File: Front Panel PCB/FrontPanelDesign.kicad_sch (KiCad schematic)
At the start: 37 parts, among them J1 Conn_01x03_Pin, U1 TL081, U2 TL081, U3 TL081, U4 TL081, U5 TL081, U6 TL081

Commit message: Power Supplies Schematic Designed
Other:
- company: (none) -> University of Stellenbosch
- title: (none) -> Equiliser
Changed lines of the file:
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@@
 	(generator_version "10.0")
 	(paper "A3")
+	(title_block
+		(title "Equiliser")
+		(date "2026-06-02")
+		(rev "Rev A")
+		(company "University of Stellenbosch")
+		(comment 1 "Author: Karl Johan Hofmeyr")
+		(comment 2 "Skripsie Project")
+		(comment 3 "BEng - Mechatronic (4th Year)")
+	)
 	(junction
 		(at 306.07 104.14)

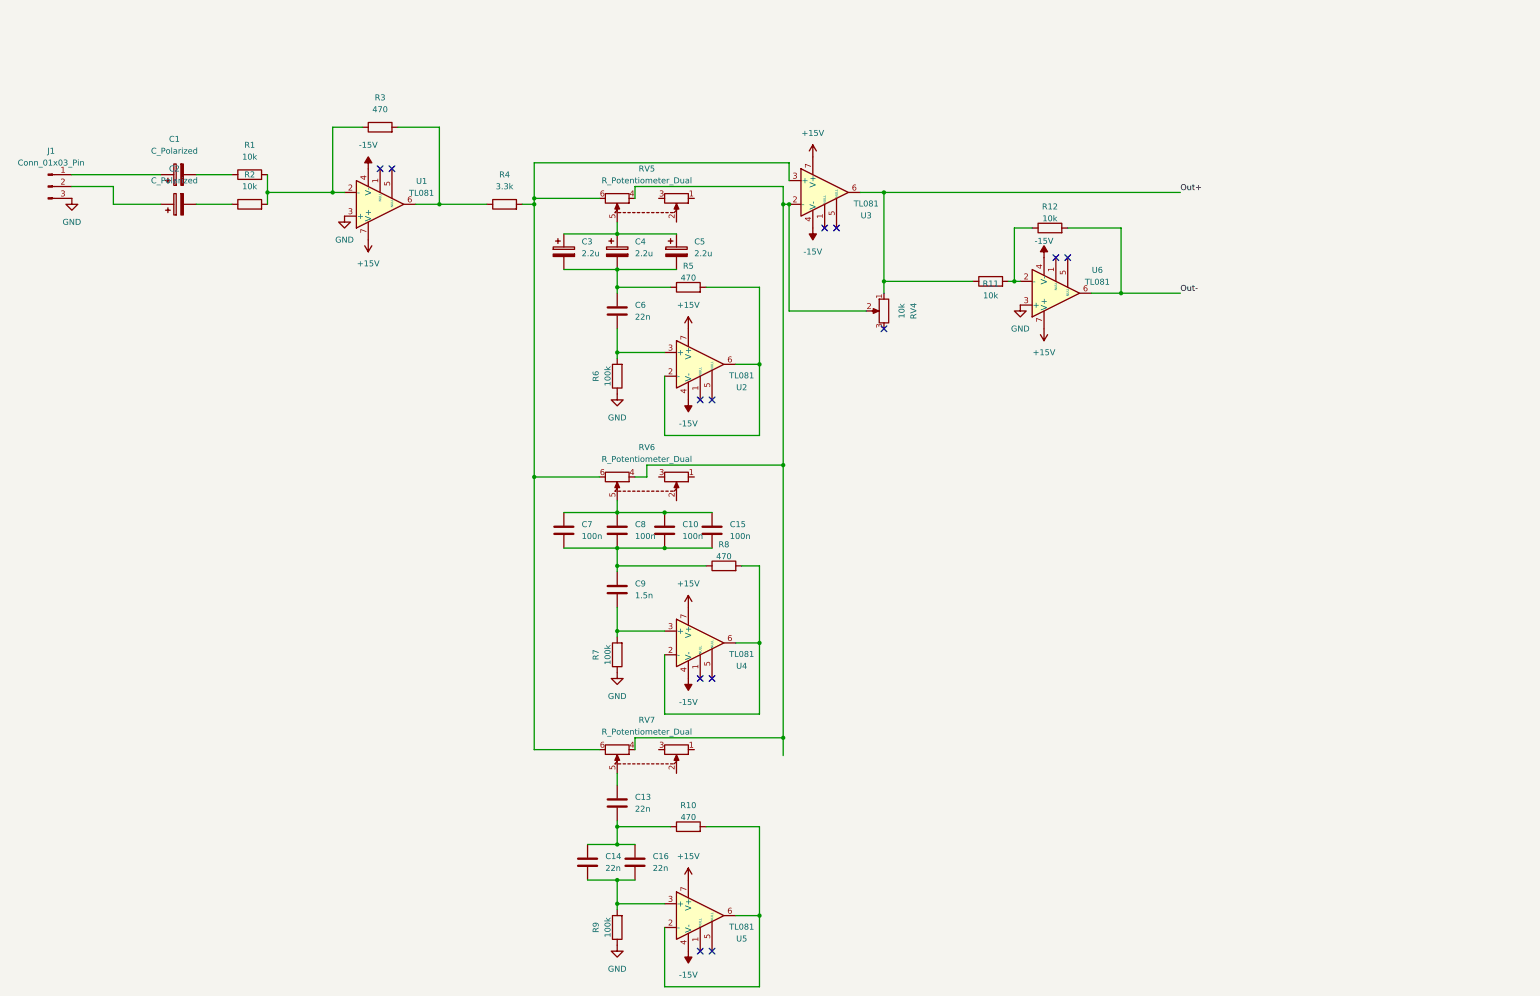
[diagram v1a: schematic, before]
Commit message: Output Stage Schematic Created and complete. Next: Integrate STM32
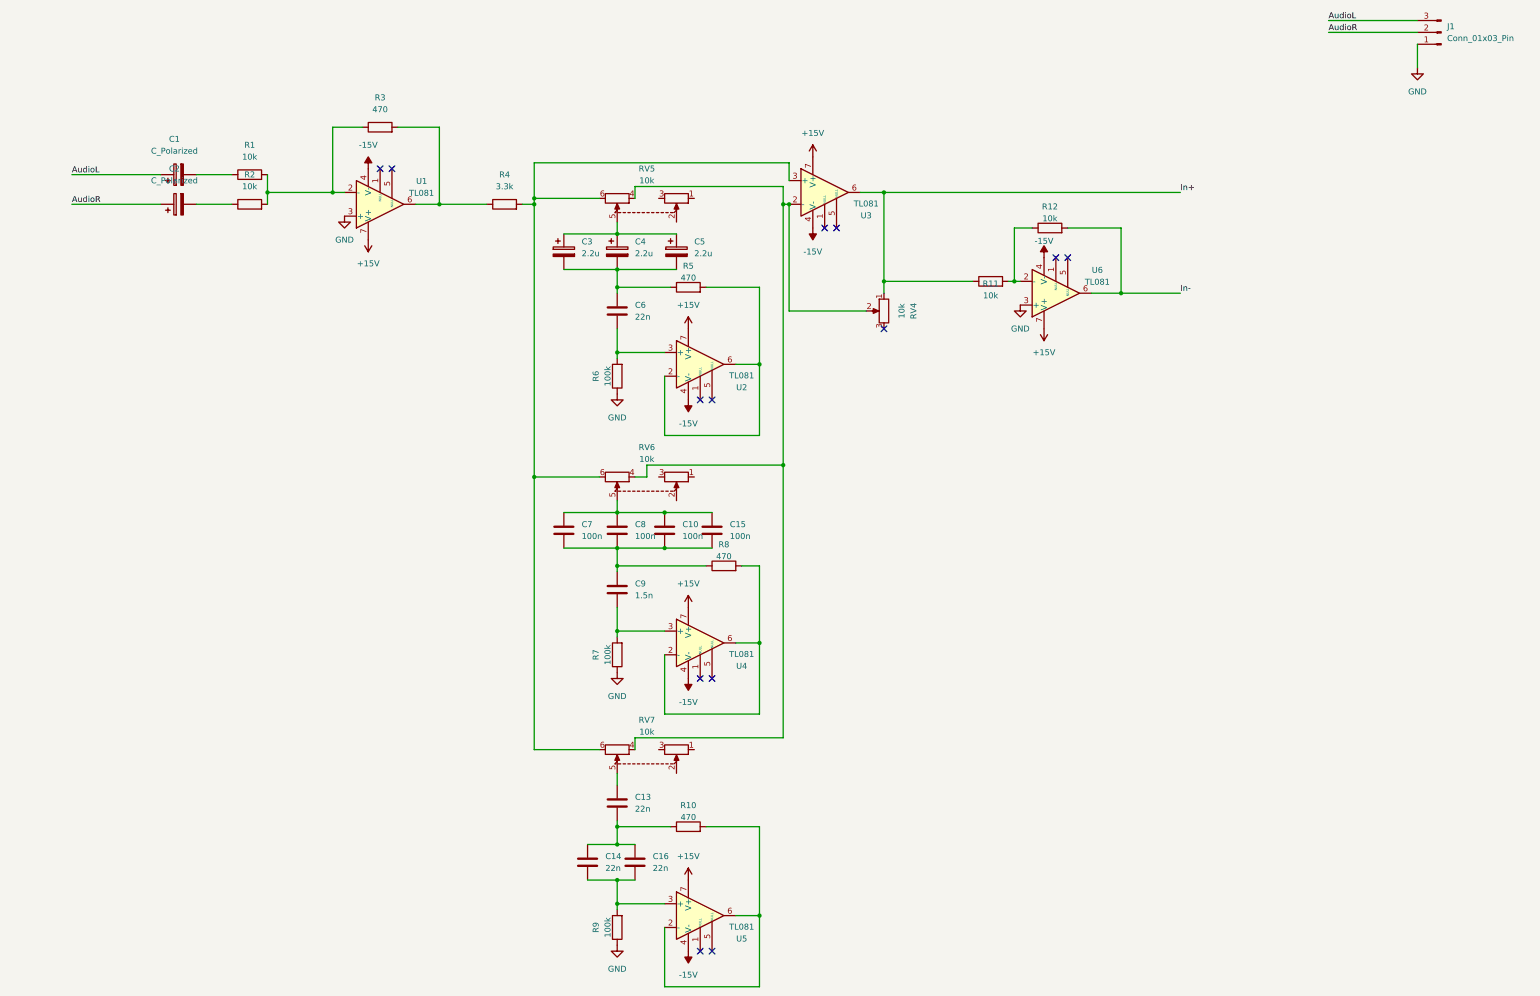
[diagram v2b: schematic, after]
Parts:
- RV5, RV6, RV7: value R_Potentiometer_Dual -> 10k
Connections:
- net GND: now also J1.1 (Pin_1); no longer J1.3 (Pin_3)
- net AudioL: now reaches C1.1
- net AudioL: now also J1.3 (Pin_3); no longer J1.1 (Pin_1)
- net AudioR: now reaches C2.1, J1.2 (Pin_2)
- net Out+ renamed In+
- net Out- renamed In-

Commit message: Bill of materials ETC finalised, selecting footprints next
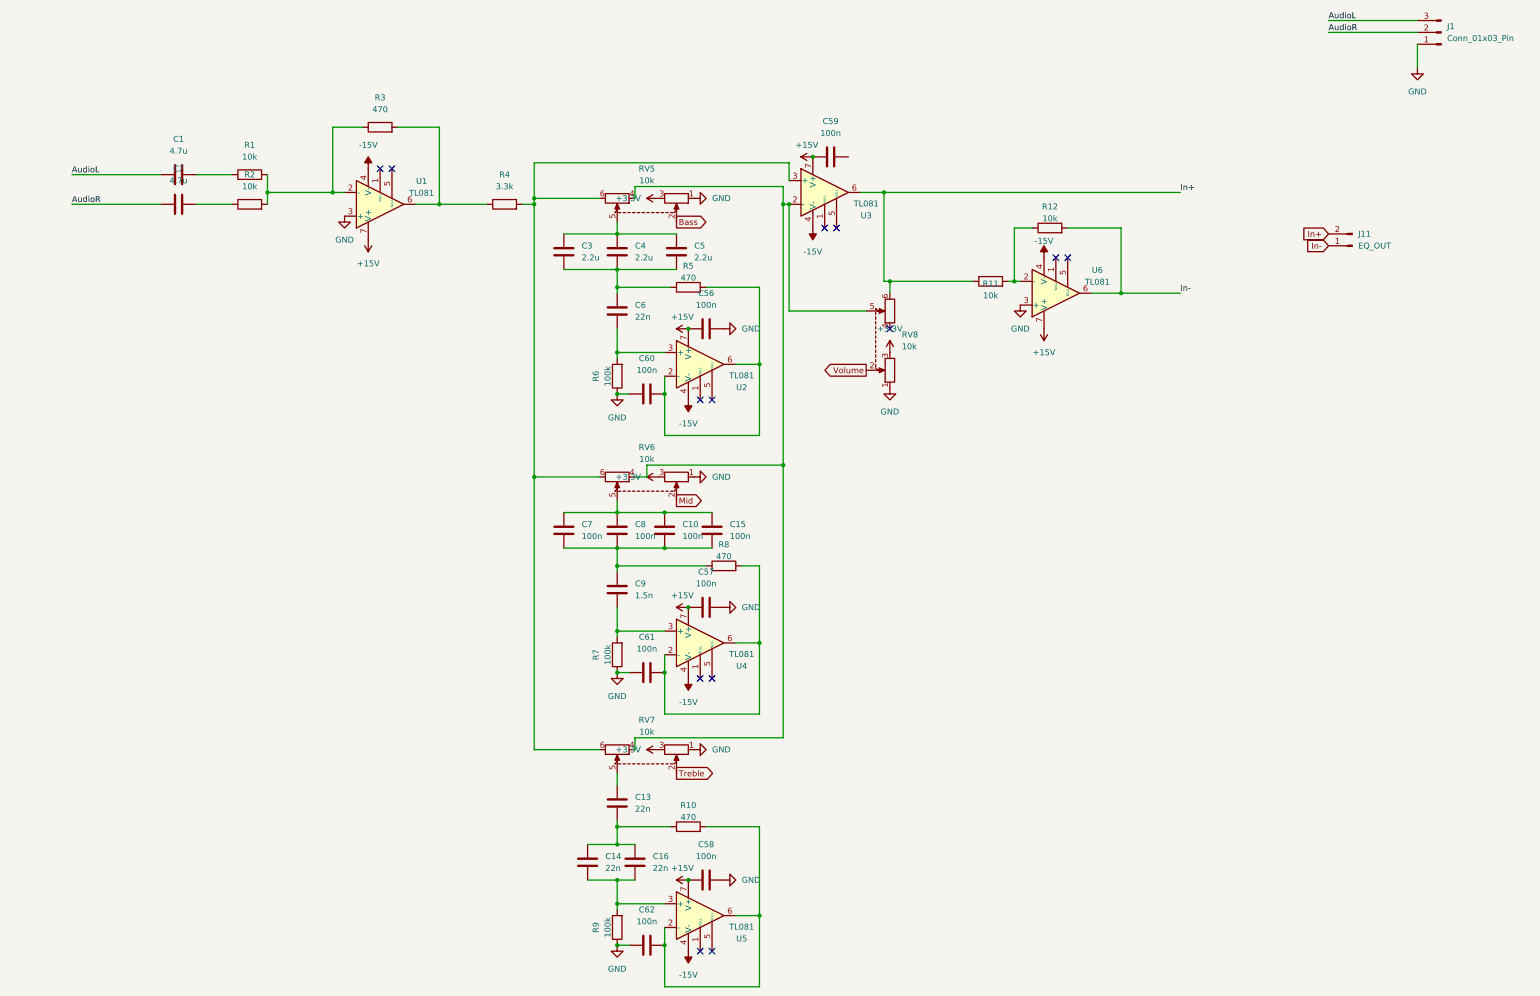
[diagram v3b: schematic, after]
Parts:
- removed C1, C2: C_Polarized, symbol Device:C_Polarized
- removed C3, C4, C5: 2.2u, symbol Device:C_Polarized
- removed RV4: 10k, symbol Device:R_Potentiometer
- added C1, C2: 4.7u, symbol Device:C
- added C3, C4, C5: 2.2u, symbol Device:C
- added C56, C57, C58, C59, C60, C61, C62: 100n, symbol Device:C
- added J11: EQ_OUT, symbol Connector:Conn_01x02_Pin
- added RV8: 10k, symbol Device:R_Potentiometer_Dual
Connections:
- net +15V: now also C56.2, C57.2, C58.2, C59.2
- net AudioL: now also C1.1
- net AudioR: now also C2.1
- net GND: now also RV5.1, RV6.1, RV7.1, C56.1, C57.1, C58.1, C60.2, C61.2, C62.2, RV8.1
- net In+: now also J11.2 (Pin_2), RV8.6
- net In-: now also J11.1 (Pin_1)
- net at R10.2, U5.2 (-), U5.6: now also C62.1
- net at RV5.4, RV6.4, RV7.4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: now also RV8.5
- net at C6.1, R5.1: now also C3.1, C4.1, C5.1
- net at RV5.5: now also C3.2, C4.2, C5.2
- net at R5.2, U2.2 (-), U2.6: now also C60.1
- net Treble: now reaches RV7.2
- net +3.3V: now reaches RV7.3
- net +3.3V: now also RV5.3, RV6.3, RV8.3
- net Bass: now reaches RV5.2
- net at R2.1: now also C2.2
- net Mid: now reaches RV6.2
- net at R8.2, U4.2 (-), U4.6: now also C61.1
- net at R1.1: now also C1.2
- new net Volume: RV8.2
